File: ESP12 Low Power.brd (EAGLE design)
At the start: 99.8 x 49.8 mm, 48 parts, among them Q1 FDN338P, U2 AP2112K-3.3TRG1

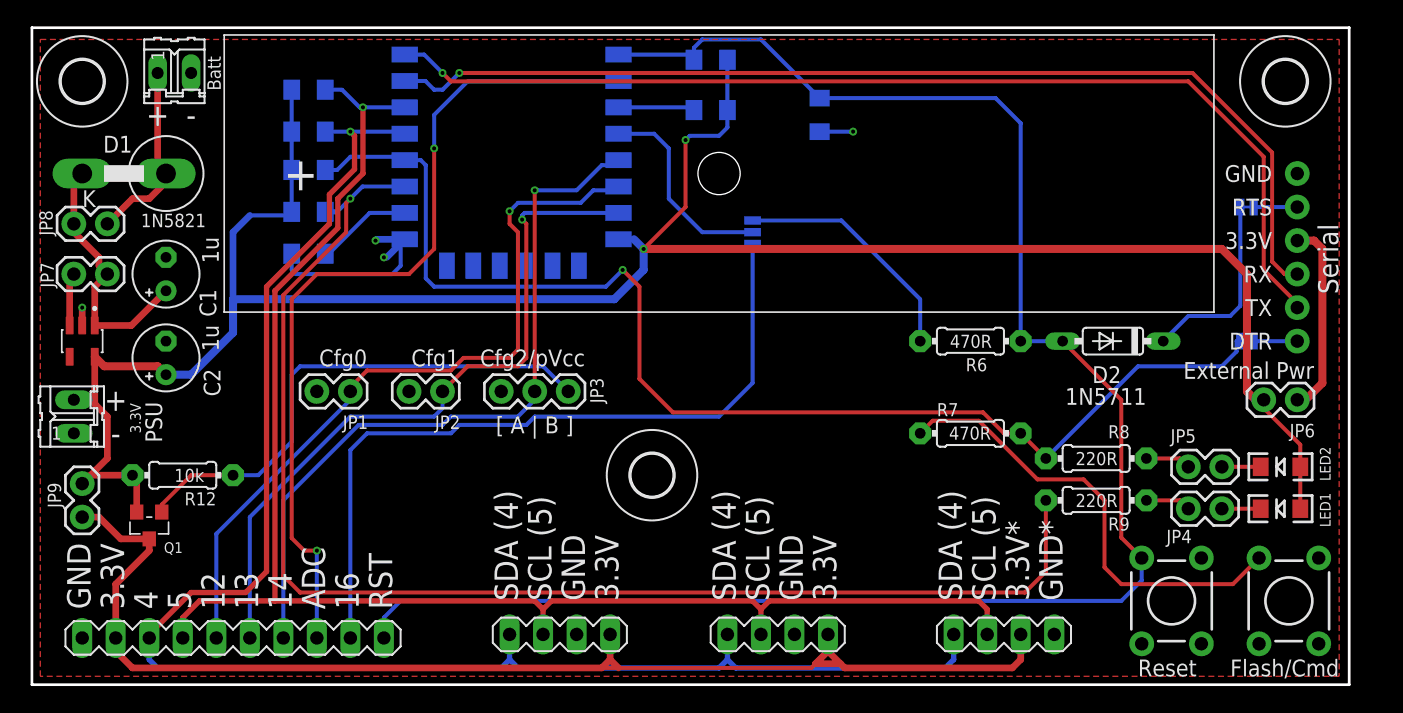
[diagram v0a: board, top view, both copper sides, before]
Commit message: move some things away from screw holes on board
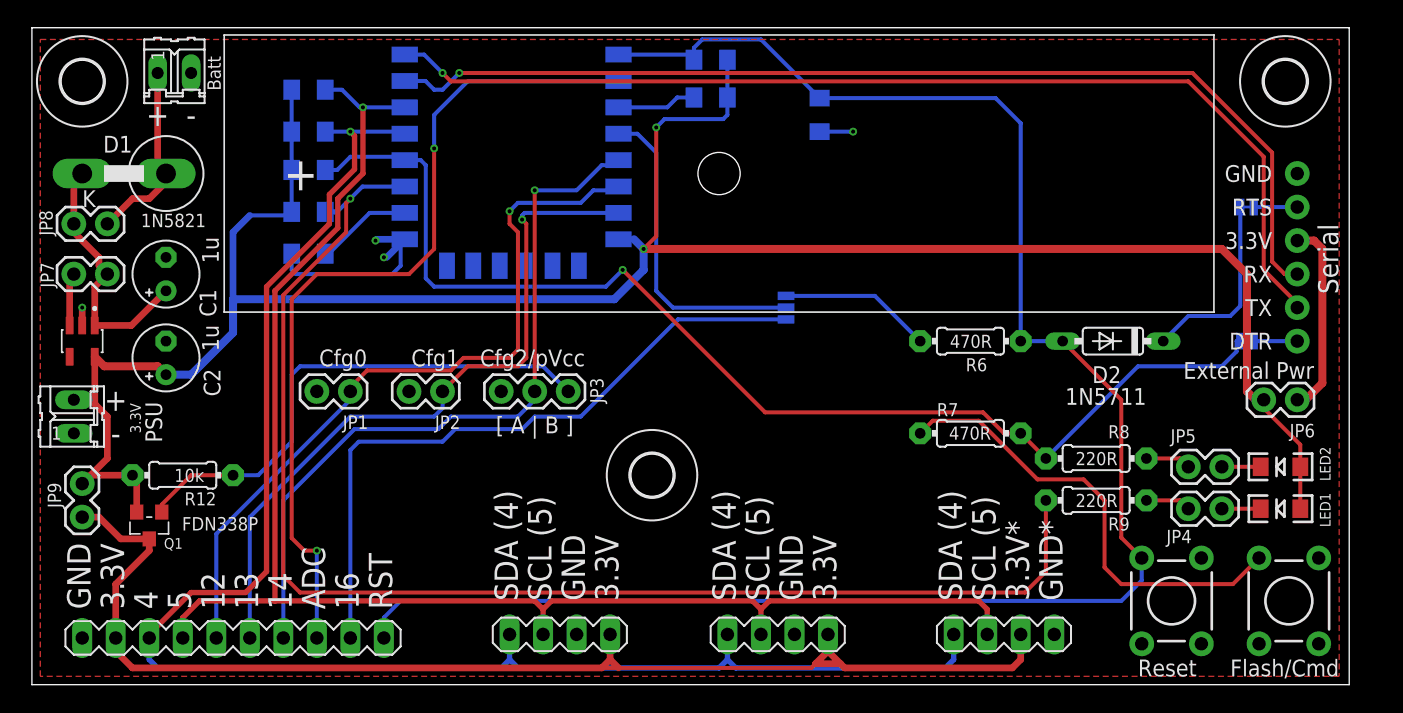
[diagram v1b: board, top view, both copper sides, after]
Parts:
- moved SJ1 6.25 mm to (57.1, 28.6)
- moved R4 0.95 mm to (51.4, 44.5)
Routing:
- net N$12: track 15.5 -> 24.3 mm
- net N$11: track 18.3 -> 11.6 mm
- net GPIO16: track 57.4 -> 51.4 mm
- net GPIO0: track 93.5 -> 89.4 mm
- net VCC: track 174.3 -> 175.6 mm
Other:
- board text added: "C1"
- board text added: "C2"
- board text added: "C3"
- board text added: "D1"
- board text added: "D2"
- board text added: "JP1"
- board text added: "JP2"
- board text added: "JP3"
- board text added: "JP4"
- board text added: "JP5"
- board text added: "JP6"
- board text added: "JP7"
- board text added: "JP8"
- board text added: "JP9"
- board text added: "LED1"
- board text added: "LED2"
- board text added: "Q1"
- board text added: "R1"
- board text added: "R10"
- board text added: "R11"
- board text added: "R12"
- board text added: "R2"
- board text added: "R3"
- board text added: "R4"
- board text added: "R5"
- board text added: "R6"
- board text added: "R7"
- board text added: "R8"
- board text added: "R9"
- board text added: "S1"
- board text added: "S2"
- board text added: "SJ1"
- board text added: "SJ2"
- board text added: "SJ3"
- board text added: "SJR1"
- board text added: "SL1"
- board text added: "SL2"
- board text added: "U$1"
- board text added: "U2"

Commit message: Changes for v1.1 See Github issues
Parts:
- added EP3: (no value), Master 2016:FCI_USB_B_SMD
- added S3: Cfg1 Reed, Master 2016:REED_SWITCH_PTH
- added S4: Rst Reed, Master 2016:REED_SWITCH_PTH
- added SJ4, SJ5: SOLDERJUMPERTRACE, Master 2016:SJ_2S-TRACE
- added SW1: SWITCH_SPDTMULTICOMP_MS2, Master 2016:MULTICOMP_2MS
- moved R12 13.1 mm to (19.7, 26.0)
- moved Q1 9.92 mm to (15.2, 19.7)
- moved JP9 8.89 mm to (12.7, 15.2), turned to 0 degrees
- moved C3 2.54 mm to (59.7, 40.6), turned to 90 degrees
- moved LOGO1 2.29 mm to (84.5, 45.1), turned to 90 degrees
- moved S1 0.64 mm to (94.6, 6.35)
- moved JP6 0.64 mm to (95.9, 21.0)
- moved SJ3 0.63 mm to (92.1, 36.8)
- moved SV1 0.63 mm to (95.9, 39.4)
- renumbered SL1 to EP1, SL2 to EP2
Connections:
- new net V_REG: C2.+, EP2.2, SW1.P$3, U2.5
- net GND: now also EP3.GND, S3.P$1, S4.P$1
- net GPIO13: now also S3.P$2
- net N$13: now also EP3.VCC
- net N$3: now also SJ4.1
- net N$8: now also SJ4.2
- net RST: now also S4.P$2
- net VCC: now also SJ5.2, SW1.P$2; no longer C2.+, EP2.2, U2.5
- net VCC@P: now also SJ5.1
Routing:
- net N$13: track 14.3 -> 90.2 mm, vias 0 -> 1
- net GND: track 20.2 -> 63.4 mm, vias 4 -> 3
- net V_REG: track 0.00 -> 20.1 mm
- net N$17: track 39.5 -> 30.1 mm, vias 0 -> 1
- net GPIO16: track 51.4 -> 43.2 mm
- net A0: track 64.6 -> 72.4 mm
- net VCC: track 175.6 -> 168.5 mm
- net VCC@P: track 94.5 -> 99.8 mm
- net GPIO14: track 55.8 -> 51.2 mm
- net GPIO13: track 54.2 -> 51.9 mm
- net N$3: track 4.03 -> 5.80 mm
- net N$8: track 19.7 -> 21.5 mm
- net N$14: track 14.4 -> 15.1 mm
- net RXD: track 79.6 -> 78.9 mm
- net N$9: track 14.8 -> 15.3 mm
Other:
- board text added: "A | B"
- board text added: "AP2112"
- board text added: "Adam Cooper 2023 Version 1.1"
- board text added: "Cfg1 Reed"
- board text added: "EP1"
- board text added: "EP2"
- board text added: "GPIO"
- board text added: "ON"
- board text added: "Power"
- board text added: "Reset Reed"
- board text removed: "Adam Cooper 2023 Version 1.0"
- board text removed: "SL1"
- board text removed: "SL2"
